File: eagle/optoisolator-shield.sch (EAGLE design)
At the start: 48 parts, among them Q1 MMBT2222ALT3G, Q2 MMBT2222ALT3G, Q3 MMBT2222ALT3G, Q4 MMBT2222ALT3G, Q5 MMBT2222ALT3G, Q6 MMBT2222ALT3G, U1 OPTO, U2 OPTO, U3 OPTO

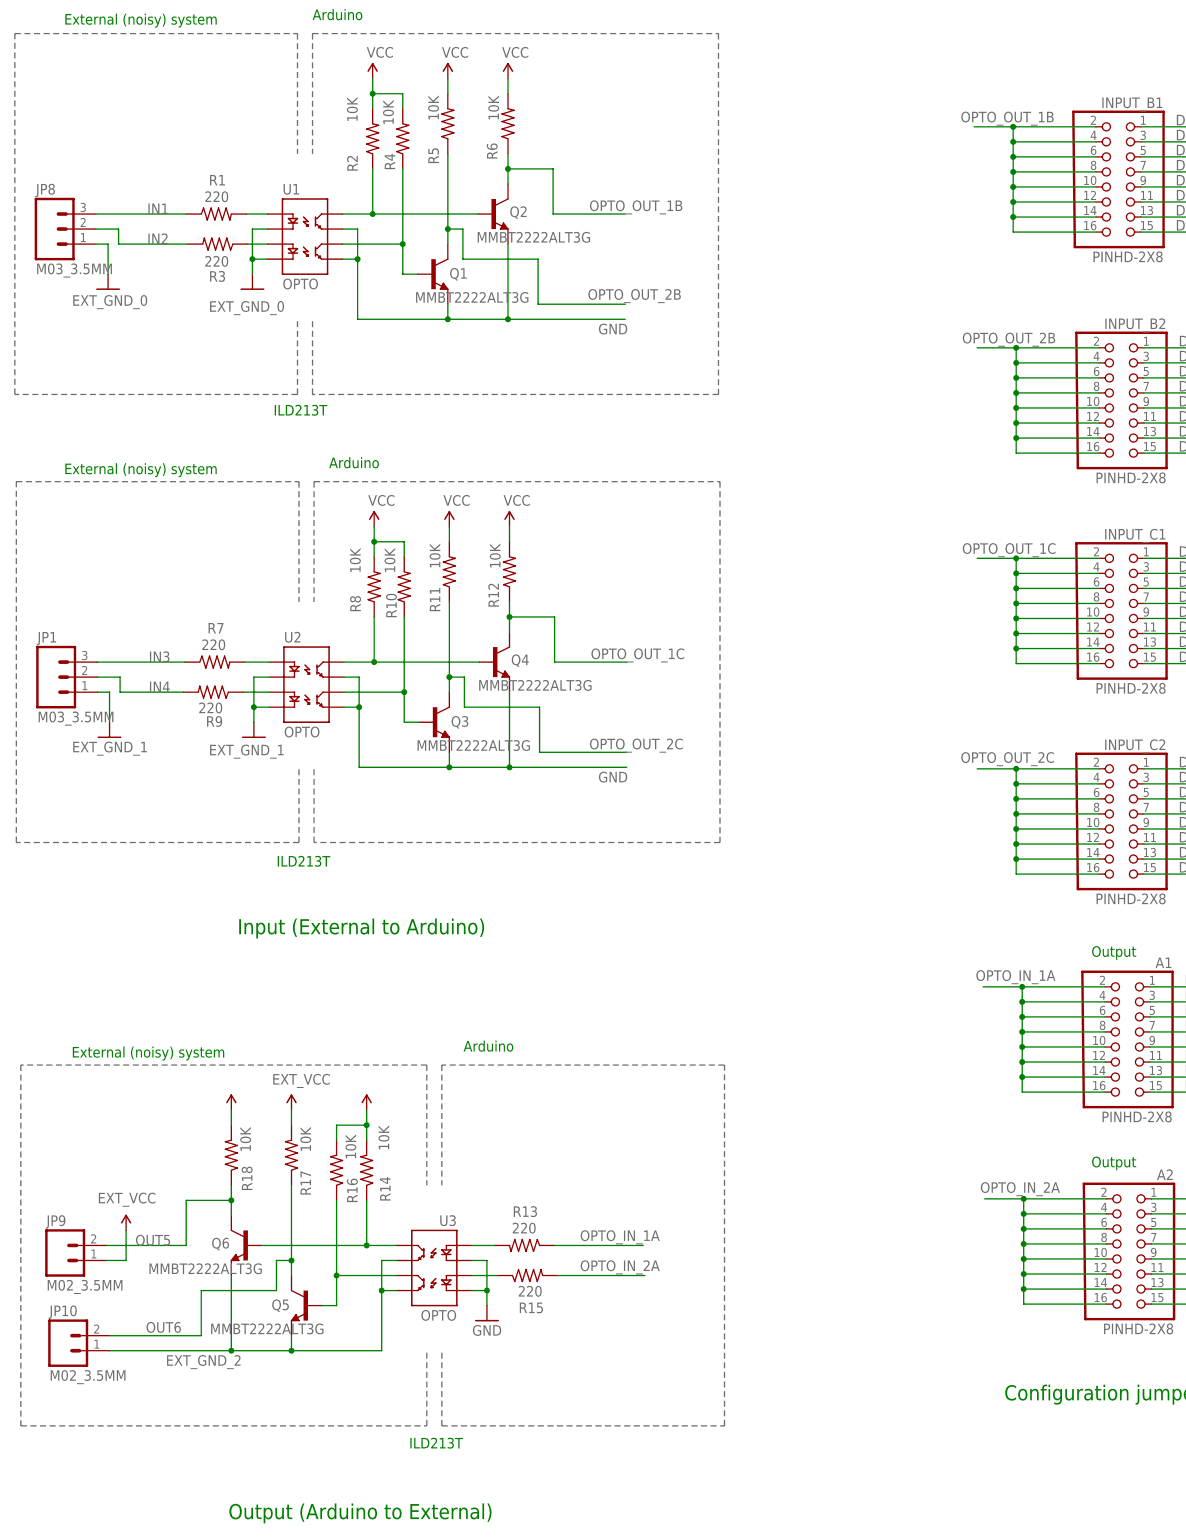
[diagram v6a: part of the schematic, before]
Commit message: updated schematic renaming inputs/outputs 1A... to A1... for clarity
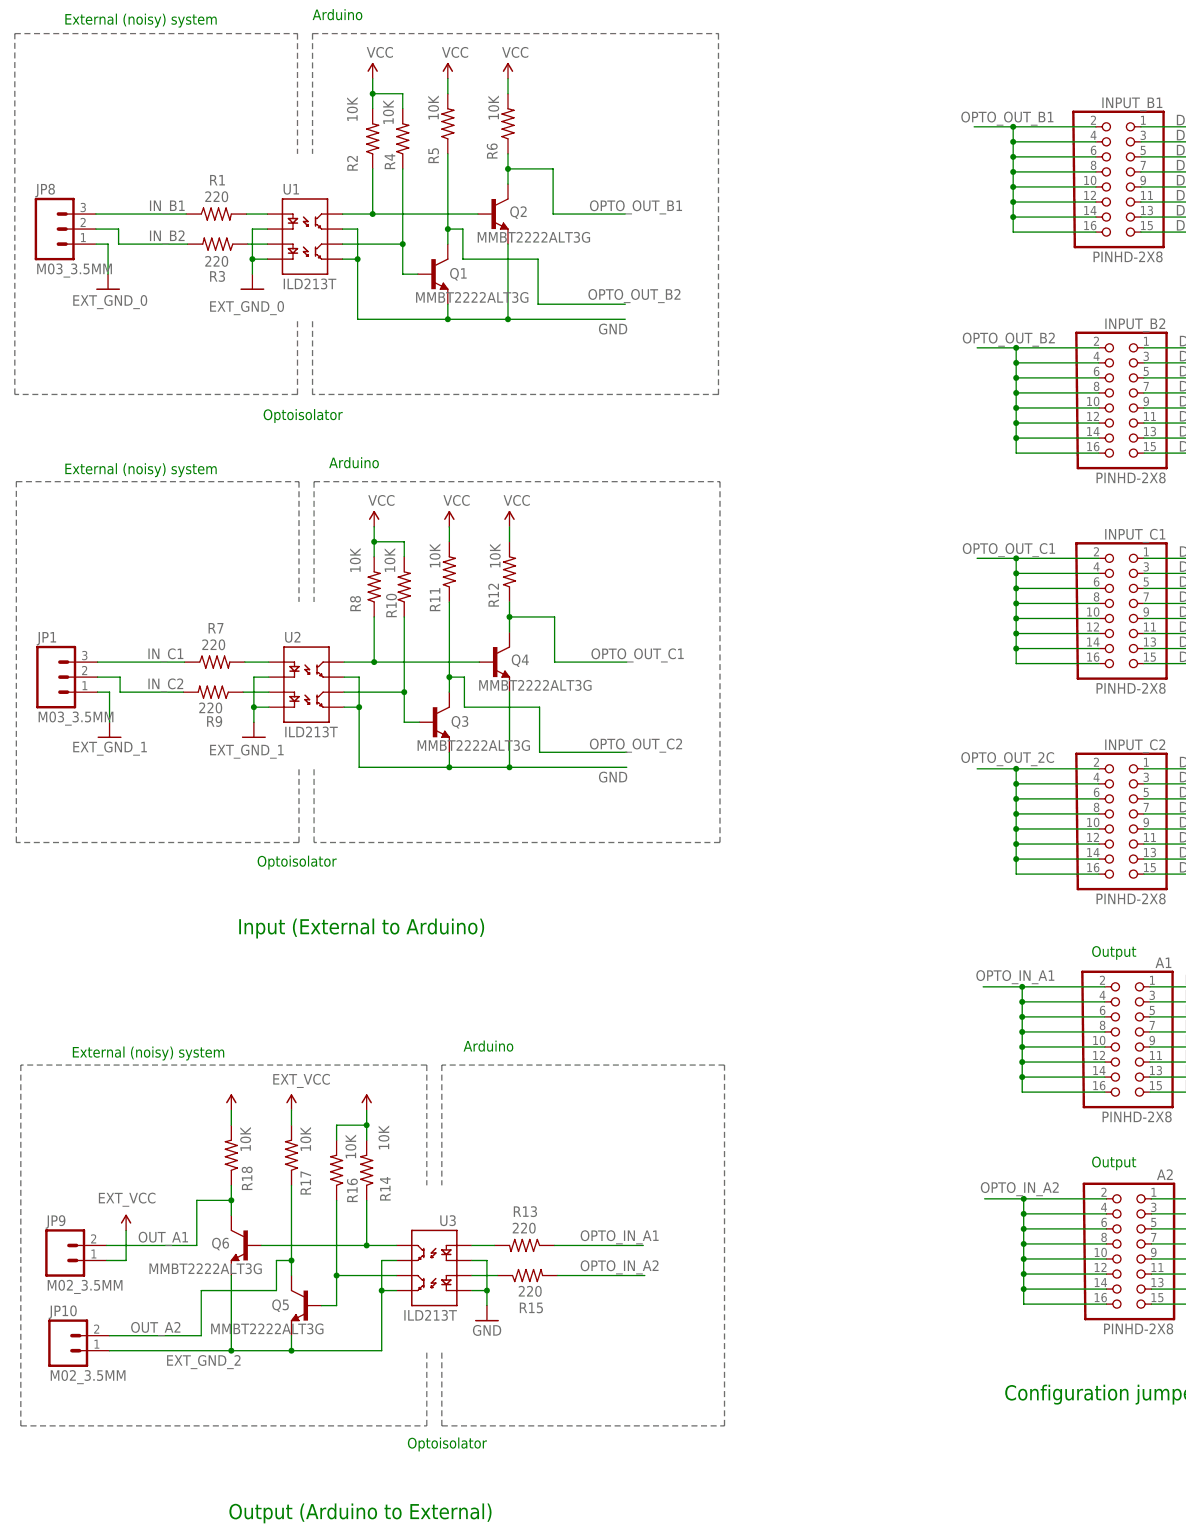
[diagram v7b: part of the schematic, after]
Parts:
- U1, U2, U3: value OPTO -> ILD213T
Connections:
- net IN1 renamed IN_B1
- net IN2 renamed IN_B2
- net IN3 renamed IN_C1
- net IN4 renamed IN_C2
- net OPTO_IN_1A renamed OPTO_IN_A1
- net OPTO_IN_2A renamed OPTO_IN_A2
- net OPTO_OUT_1B renamed OPTO_OUT_B1
- net OPTO_OUT_1C renamed OPTO_OUT_C1
- net OPTO_OUT_2B renamed OPTO_OUT_B2
- net OUT5 renamed OUT_A1
- net OUT6 renamed OUT_A2
- new net OPTO_OUT_C2: Q3.C, R11.1
- net OPTO_OUT_2C: no longer Q3.C, R11.1
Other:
- note added: "Optoisolator"
- note removed: "ILD213T"
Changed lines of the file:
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@@
 <part name="U$6" library="adafruit" deviceset="FIDUCIAL" device=""/>
 <part name="U$2" library="adafruit" deviceset="FIDUCIAL" device=""/>
-<part name="U2" library="SparkFun" deviceset="OPTOISOLATOR-2" device="SOIC8" value="OPTO"/>
+<part name="U2" library="SparkFun" deviceset="OPTOISOLATOR-2" device="SOIC8" value="ILD213T"/>
 <part name="R7" library="SparkFun-Passives" deviceset="RESISTOR" device="0603-RES" value="220"/>
 <part name="R8" library="SparkFun-Passives" deviceset="RESISTOR" device="0603-RES" value="10K"/>
@@
 <part name="INPUT_C2" library="headers" deviceset="PINHD-2X8" device=""/>
 <part name="JP1" library="SparkFun-Connectors" deviceset="M03" device="SCREW" value="M03_3.5MM"/>
-<part name="U1" library="SparkFun" deviceset="OPTOISOLATOR-2" device="SOIC8" value="OPTO"/>
+<part name="U1" library="SparkFun" deviceset="OPTOISOLATOR-2" device="SOIC8" value="ILD213T"/>
 <part name="R1" library="SparkFun-Passives" deviceset="RESISTOR" device="0603-RES" value="220"/>
 <part name="R2" library="SparkFun-Passives" deviceset="RESISTOR" device="0603-RES" value="10K"/>
@@
 <part name="P+4" library="SparkFun" deviceset="VCC" device="" value="VCC"/>
 <part name="JP8" library="SparkFun-Connectors" deviceset="M03" device="SCREW" value="M03_3.5MM"/>
-<part name="U3" library="SparkFun" deviceset="OPTOISOLATOR-2" device="SOIC8" value="OPTO"/>
+<part name="U3" library="SparkFun" deviceset="OPTOISOLATOR-2" device="SOIC8" value="ILD213T"/>
 <part name="R13" library="SparkFun-Passives" deviceset="RESISTOR" device="0603-RES" value="220"/>
 <part name="R14" library="SparkFun-Passives" deviceset="RESISTOR" device="0603-RES" value="10K"/>
@@
 <wire x1="143.002" y1="128.524" x2="74.422" y2="128.524" width="0.2032" layer="95" style="shortdash"/>
 <wire x1="74.422" y1="128.524" x2="74.422" y2="141.224" width="0.2032" layer="95" style="shortdash"/>
-<text x="68.072" y="124.46" size="1.778" layer="91">ILD213T</text>
+<text x="64.77" y="124.46" size="1.778" layer="91">Optoisolator</text>
 <text x="356.616" y="254" size="1.524" layer="91">SCL1</text>
 <text x="356.616" y="251.46" size="1.524" layer="91">SDA1</text>
@@
 <wire x1="142.748" y1="204.216" x2="74.168" y2="204.216" width="0.2032" layer="95" style="shortdash"/>
 <wire x1="74.168" y1="204.216" x2="74.168" y2="216.916" width="0.2032" layer="95" style="shortdash"/>
-<text x="67.564" y="200.66" size="1.778" layer="91">ILD213T</text>
+<text x="65.786" y="199.898" size="1.778" layer="91">Optoisolator</text>
 <text x="74.168" y="267.462" size="1.778" layer="91">Arduino</text>
 <text x="76.962" y="191.77" size="1.778" layer="91">Arduino</text>
@@
 <wire x1="24.892" y1="29.972" x2="93.472" y2="29.972" width="0.2032" layer="95" style="shortdash"/>
 <wire x1="93.472" y1="29.972" x2="93.472" y2="42.672" width="0.2032" layer="95" style="shortdash"/>
-<text x="99.568" y="26.162" size="1.778" layer="91" rot="MR0">ILD213T</text>
+<text x="103.632" y="26.162" size="1.778" layer="91" rot="MR0">Optoisolator</text>
 <text x="59.436" y="92.202" size="1.778" layer="91" rot="MR0">External (noisy) system</text>
 <text x="108.204" y="93.218" size="1.778" layer="91" rot="MR0">Arduino</text>
@@
 </segment>
 </net>
-<net name="IN2" class="0">
+<net name="IN_B2" class="0">
 <segment>
 <wire x1="41.402" y1="229.616" x2="53.086" y2="229.616" width="0.1524" layer="91"/>
-<label x="46.228" y="229.616" size="1.778" layer="95"/>
+<label x="46.482" y="230.124" size="1.778" layer="95"/>
 <pinref part="R3" gate="G$1" pin="2"/>
 <pinref part="JP8" gate="G$1" pin="2"/>
@@
 </segment>
 </net>
-<net name="IN1" class="0">
+<net name="IN_B1" class="0">
 <segment>
 <wire x1="52.832" y1="234.696" x2="37.592" y2="234.696" width="0.1524" layer="91"/>
-<label x="46.228" y="234.696" size="1.778" layer="95"/>
+<label x="46.482" y="235.204" size="1.778" layer="95"/>
 <pinref part="R1" gate="G$1" pin="1"/>
 <pinref part="JP8" gate="G$1" pin="3"/>
@@
 </segment>
 </net>
-<net name="IN3" class="0">
+<net name="IN_C1" class="0">
 <segment>
 <wire x1="52.578" y1="159.004" x2="37.846" y2="159.004" width="0.1524" layer="91"/>
-<label x="46.482" y="159.004" size="1.778" layer="95"/>
+<label x="46.228" y="159.512" size="1.778" layer="95"/>
 <pinref part="R7" gate="G$1" pin="1"/>
 <pinref part="JP1" gate="G$1" pin="3"/>
 </segment>
 </net>
-<net name="IN4" class="0">
+<net name="IN_C2" class="0">
 <segment>
 <wire x1="41.656" y1="153.924" x2="52.324" y2="153.924" width="0.1524" layer="91"/>
-<label x="46.482" y="153.924" size="1.778" layer="95"/>
+<label x="46.228" y="154.432" size="1.778" layer="95"/>
 <pinref part="R9" gate="G$1" pin="2"/>
 <pinref part="JP1" gate="G$1" pin="2"/>
@@
 </segment>
 </net>
-<net name="OUT5" class="0">
+<net name="OUT_A1" class="0">
 <segment>
 <wire x1="60.452" y1="70.612" x2="60.452" y2="68.072" width="0.1524" layer="91"/>
 <wire x1="60.452" y1="68.072" x2="60.452" y2="65.532" width="0.1524" layer="91"/>
-<wire x1="60.452" y1="68.072" x2="52.832" y2="68.072" width="0.1524" layer="91"/>
-<wire x1="52.832" y1="68.072" x2="52.832" y2="60.452" width="0.1524" layer="91"/>
-<wire x1="52.832" y1="60.452" x2="39.37" y2="60.452" width="0.1524" layer="91"/>
+<wire x1="60.452" y1="68.072" x2="54.61" y2="68.072" width="0.1524" layer="91"/>
+<wire x1="54.61" y1="68.072" x2="54.61" y2="60.452" width="0.1524" layer="91"/>
+<wire x1="54.61" y1="60.452" x2="39.37" y2="60.452" width="0.1524" layer="91"/>
 <junction x="60.452" y="68.072"/>
-<label x="50.292" y="60.452" size="1.778" layer="95" rot="MR0"/>
+<label x="53.34" y="60.96" size="1.778" layer="95" rot="MR0"/>
 <pinref part="Q6" gate="G$1" pin="C"/>
 <pinref part="R18" gate="G$1" pin="1"/>
@@
 </segment>
 </net>
-<net name="OUT6" class="0">
+<net name="OUT_A2" class="0">
 <segment>
 <wire x1="70.612" y1="55.372" x2="70.612" y2="57.912" width="0.1524" layer="91"/>
@@
 </segment>
 </net>
-<net name="OPTO_OUT_1B" class="0">
+<net name="OPTO_OUT_B1" class="0">
 <segment>
 <wire x1="107.188" y1="244.856" x2="107.188" y2="242.316" width="0.1524" layer="91"/>
@@
 </segment>
 </net>
-<net name="OPTO_OUT_2B" class="0">
+<net name="OPTO_OUT_B2" class="0">
 <segment>
 <wire x1="97.028" y1="229.616" x2="97.028" y2="232.156" width="0.1524" layer="91"/>
@@
 </segment>
 </net>
-<net name="OPTO_OUT_1C" class="0">
+<net name="OPTO_OUT_C1" class="0">
 <segment>
 <wire x1="107.442" y1="169.164" x2="107.442" y2="166.624" width="0.1524" layer="91"/>
@@
 <net name="OPTO_OUT_2C" class="0">
 <segment>
-<wire x1="97.282" y1="153.924" x2="97.282" y2="156.464" width="0.1524" layer="91"/>
-<wire x1="97.282" y1="156.464" x2="99.822" y2="156.464" width="0.1524" layer="91"/>
-<wire x1="99.822" y1="156.464" x2="99.822" y2="151.384" width="0.1524" layer="91"/>
-<wire x1="99.822" y1="151.384" x2="112.522" y2="151.384" width="0.1524" layer="91"/>
-<wire x1="112.522" y1="151.384" x2="112.522" y2="143.764" width="0.1524" layer="91"/>
-<wire x1="97.282" y1="169.164" x2="97.282" y2="156.464" width="0.1524" layer="91"/>
-<junction x="97.282" y="156.464"/>
-<label x="120.904" y="144.272" size="1.778" layer="95"/>
-<pinref part="Q3" gate="G$1" pin="C"/>
-<pinref part="R11" gate="G$1" pin="1"/>
-<wire x1="127.254" y1="143.764" x2="112.522" y2="143.764" width="0.1524" layer="91"/>
-</segment>
-<segment>
 <pinref part="INPUT_C2" gate="G$1" pin="2"/>
 <wire x1="207.01" y1="140.97" x2="193.04" y2="140.97" width="0.1524" layer="91"/>
@@
 </segment>
 </net>
-<net name="OPTO_IN_1A" class="0">
+<net name="OPTO_IN_A1" class="0">
 <segment>
 <wire x1="115.062" y1="60.452" x2="130.048" y2="60.452" width="0.1524" layer="91"/>
@@
 </segment>
 </net>
-<net name="OPTO_IN_2A" class="0">
+<net name="OPTO_IN_A2" class="0">
 <segment>
 <wire x1="130.302" y1="55.372" x2="115.57" y2="55.372" width="0.1524" layer="91"/>
@@
 </segment>
 </net>
+<net name="OPTO_OUT_C2" class="0">
+<segment>
+<wire x1="97.282" y1="153.924" x2="97.282" y2="156.464" width="0.1524" layer="91"/>
+<wire x1="97.282" y1="156.464" x2="99.822" y2="156.464" width="0.1524" layer="91"/>
+<wire x1="99.822" y1="156.464" x2="99.822" y2="151.384" width="0.1524" layer="91"/>
+<wire x1="99.822" y1="151.384" x2="112.522" y2="151.384" width="0.1524" layer="91"/>
+<wire x1="112.522" y1="151.384" x2="112.522" y2="143.764" width="0.1524" layer="91"/>
+<wire x1="97.282" y1="169.164" x2="97.282" y2="156.464" width="0.1524" layer="91"/>
+<junction x="97.282" y="156.464"/>
+<label x="120.904" y="144.272" size="1.778" layer="95"/>
+<pinref part="Q3" gate="G$1" pin="C"/>
+<pinref part="R11" gate="G$1" pin="1"/>
+<wire x1="127.254" y1="143.764" x2="112.522" y2="143.764" width="0.1524" layer="91"/>
+</segment>
+</net>

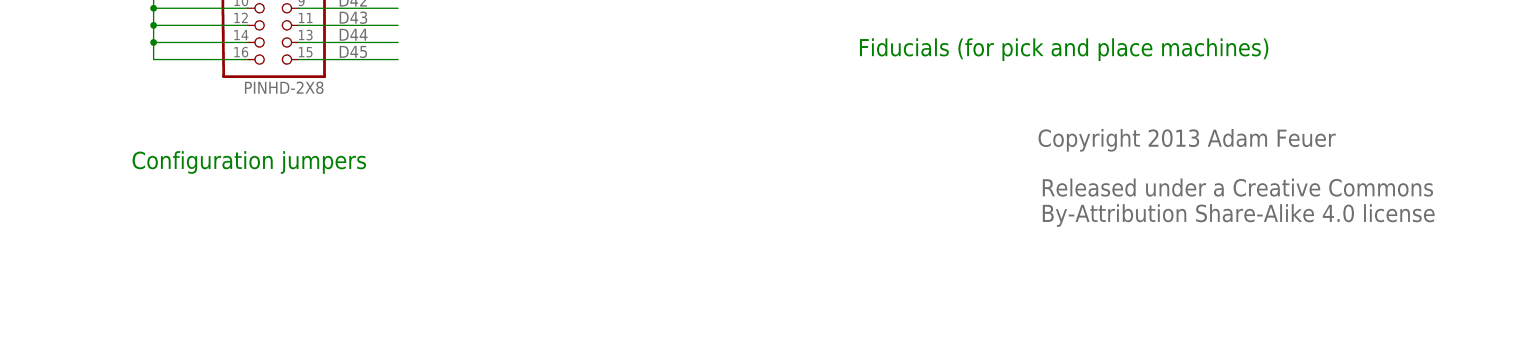
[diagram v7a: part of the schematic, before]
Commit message: added shield name to schematic
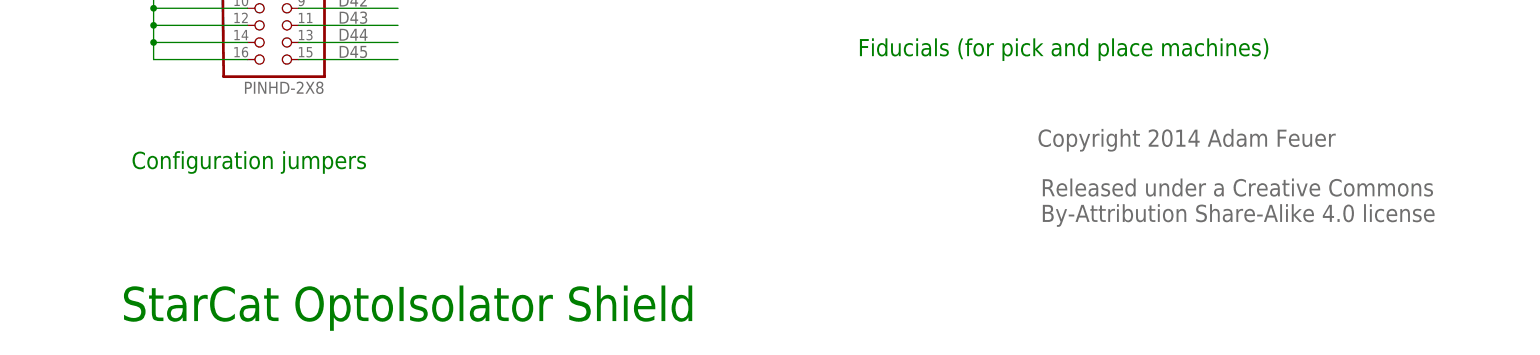
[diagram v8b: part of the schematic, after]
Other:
- note added: "Copyright 2014 Adam Feuer"
- note added: "StarCat OptoIsolator Shield"
- note removed: "Copyright 2013 Adam Feuer"
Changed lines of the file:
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@@
 <text x="326.136" y="26.416" size="2.54" layer="95">Released under a Creative Commons
 By-Attribution Share-Alike 4.0 license</text>
-<text x="325.628" y="37.592" size="2.54" layer="95">Copyright 2013 Adam Feuer</text>
+<text x="325.628" y="37.592" size="2.54" layer="95">Copyright 2014 Adam Feuer</text>
 <text x="315.468" y="84.582" size="2.54" layer="91">Shield Connectors</text>
 <text x="307.086" y="179.578" size="1.524" layer="91">A8</text>
@@
 <text x="205.74" y="109.22" size="1.778" layer="91">Output</text>
 <text x="205.74" y="73.66" size="1.778" layer="91">Output</text>
+<text x="189.484" y="11.684" size="5.08" layer="91">StarCat OptoIsolator Shield</text>
 </plain>
 <instances>
